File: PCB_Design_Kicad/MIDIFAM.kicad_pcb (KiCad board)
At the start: 2 copper layers, 58 x 87.2 mm, 61 parts, among them IC1 DAC8562SDGSR, J1 PWR_IN, J10 midi, J11 back bottom, J12 front bottom, J13 back top, J14 front top, J2 ISP connector, J3 Voct_A, J4 Trig_A, J5 Vel_A, J6 Voct_B, J7 Trig_B, J8 Vel_B, J9 adv_clock_out, SW1 re-sync, SW2 midi learn, SW3 seq. mode, U1 TL072, U2 MCP1703Ax-500xxDB, U5 6N137, U6 ATmega328-A

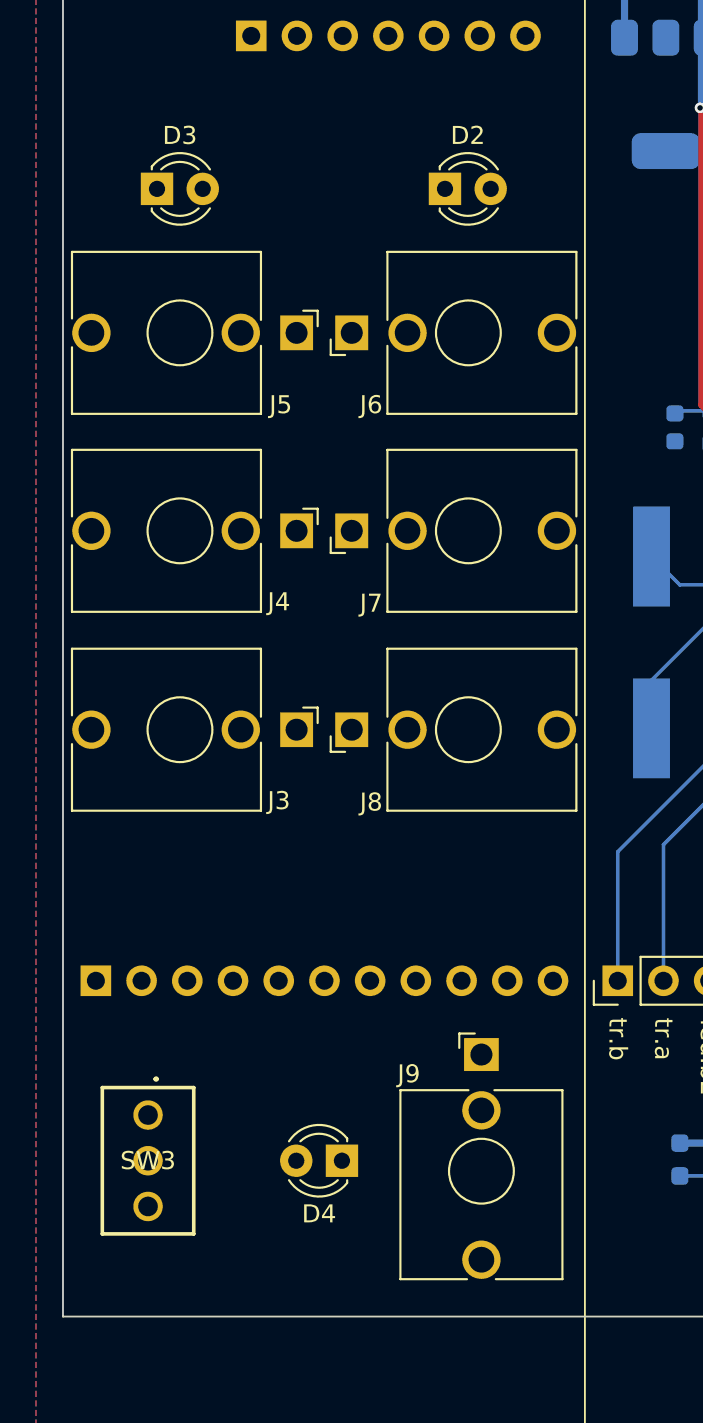
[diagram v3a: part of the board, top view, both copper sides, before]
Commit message: fix footprints and jack position
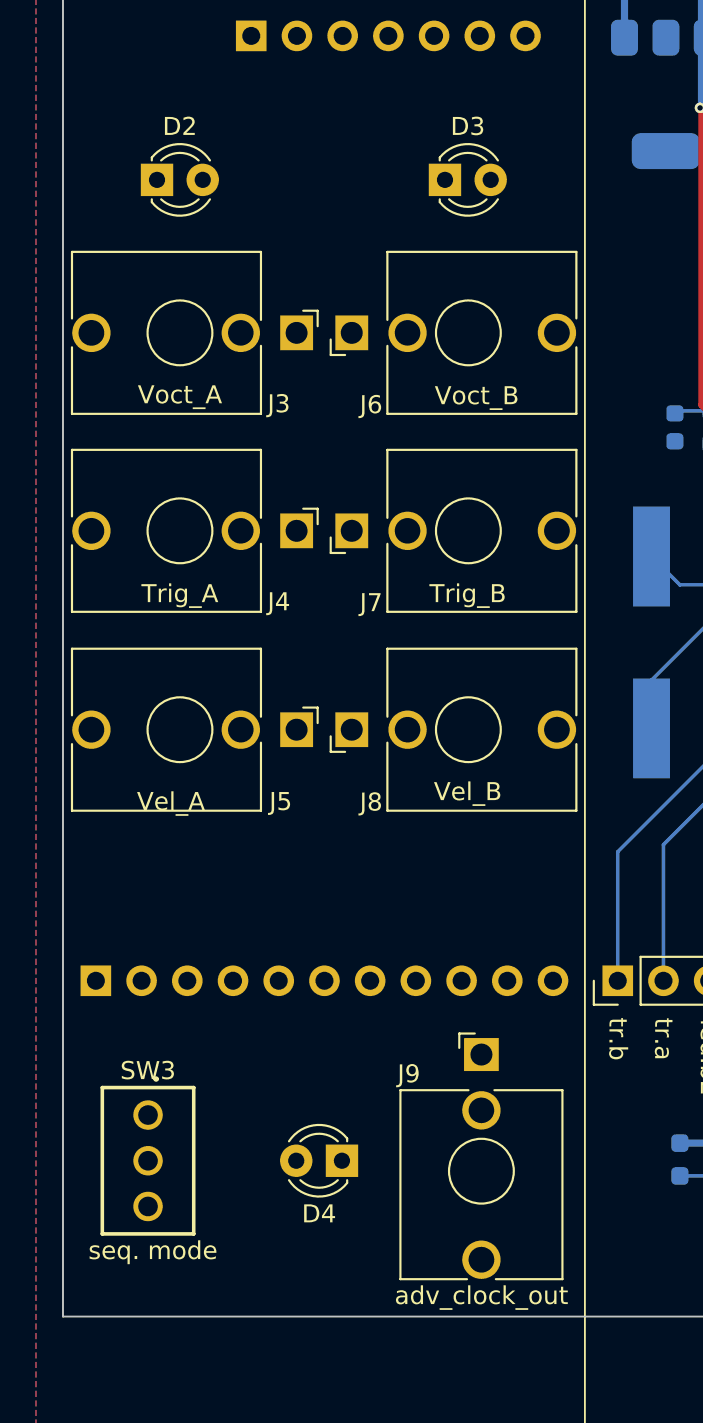
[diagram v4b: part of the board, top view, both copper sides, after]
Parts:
- moved J3 22.0 mm to (61.3, 57.5)
- moved J5 22.0 mm to (61.3, 79.5)
- moved D2 16.0 mm to (60.0, 49.0)
- moved D3 16.0 mm to (76.0, 49.0)

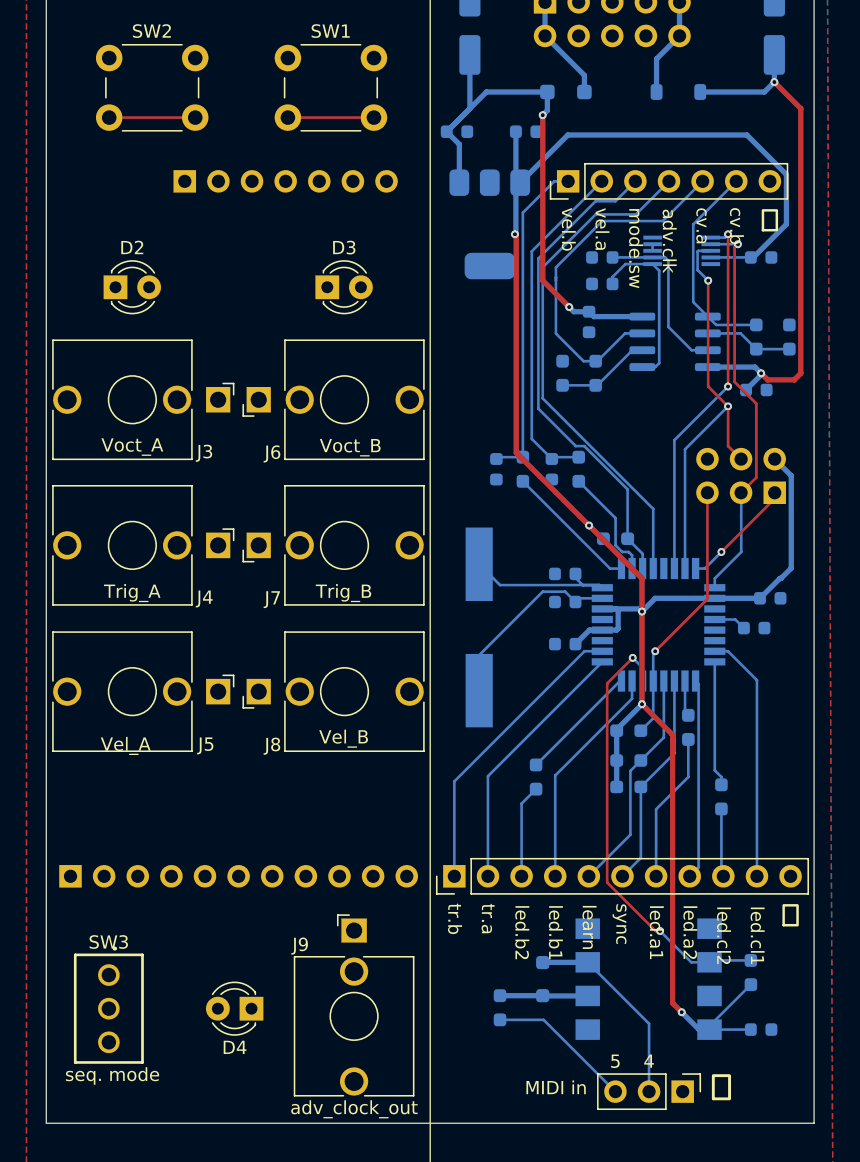
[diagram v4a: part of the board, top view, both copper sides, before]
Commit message: good routing and ground planes
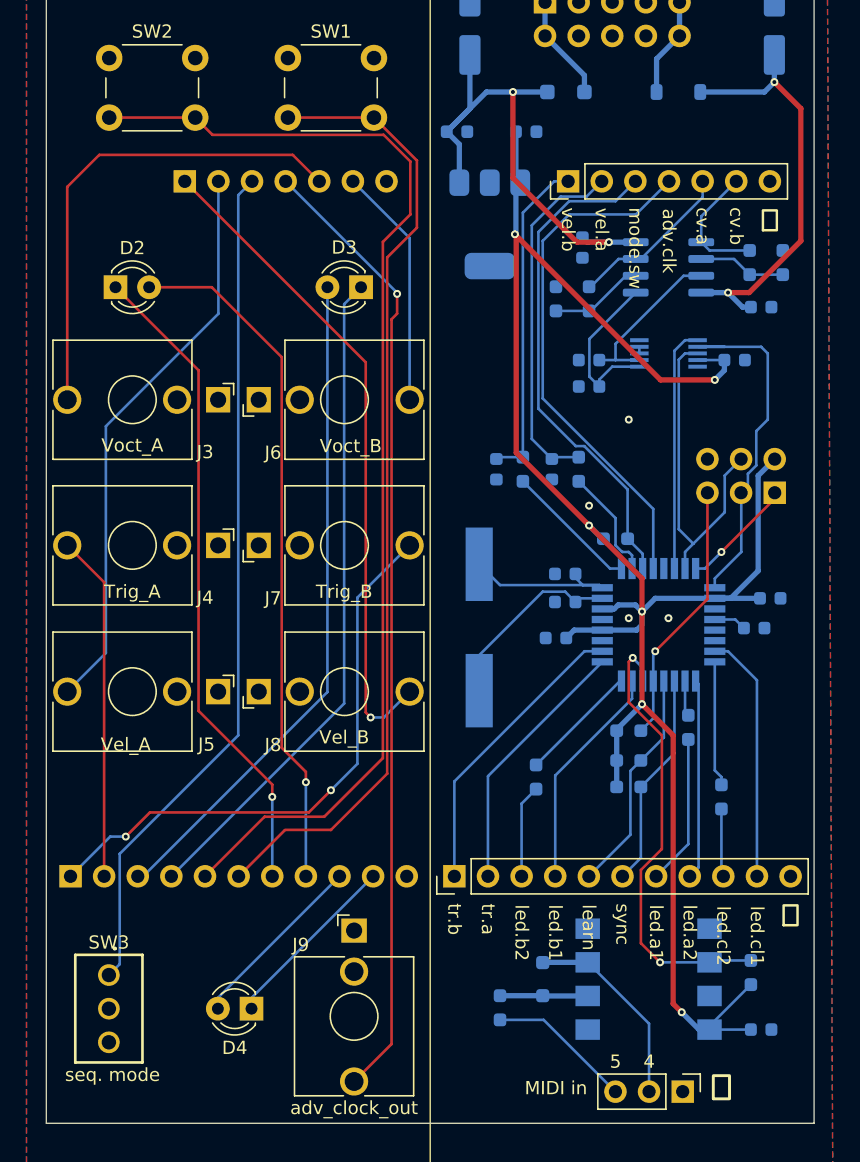
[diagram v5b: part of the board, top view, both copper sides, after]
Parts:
- moved C17 8.00 mm to (106.8, 54.5)
- moved C4 7.81 mm to (95.8, 56.5)
- moved C5 7.81 mm to (95.8, 54.5)
- moved IC1 7.81 mm to (101.8, 54.0)
- moved C12 6.27 mm to (108.8, 50.5)
- moved C10 5.65 mm to (95.3, 46.0)
- moved R1 5.65 mm to (95.8, 49.9)
- moved R2 5.65 mm to (93.3, 49.9)
- moved R3 5.65 mm to (107.9, 47.1)
- moved R4 5.65 mm to (110.4, 47.1)
- moved U1 5.65 mm to (101.8, 47.5)
- moved D3 2.55 mm to (78.5, 49.0), turned to 180 degrees
- moved C1 0.84 mm to (93.3, 75.5)
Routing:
- net /IO Control PCB/learn_sw_f: track 6.50 -> 87.2 mm
- net /IO Control PCB/adv_clock_f: track 0.00 -> 72.8 mm, vias 0 -> 1
- net /IO Control PCB/sync_sw_f: track 6.50 -> 72.8 mm
- net /IO Control PCB/seq_mode_sw: track 0.00 -> 64.4 mm
- net /IO Control PCB/led_a2_f: track 0.00 -> 52.2 mm, vias 0 -> 1
- net /IO Control PCB/led_b2_f: track 0.00 -> 50.7 mm
- net /IO Control PCB/led_b1_f: track 0.00 -> 50.4 mm
- net /IO Control PCB/vel_b_f: track 0.00 -> 50.1 mm, vias 0 -> 1
- net /IO Control PCB/led_a1_f: track 0.00 -> 49.4 mm, vias 0 -> 1
- net /IO Control PCB/trig_b_f: track 0.00 -> 43.3 mm, vias 0 -> 2
- net /IO Control PCB/vel_a_f: track 0.00 -> 43.3 mm
- net /IO Control PCB/voct_a_f: track 0.00 -> 37.0 mm
- net /IO Control PCB/trig_a_f: track 0.00 -> 26.2 mm
- net /IO Control PCB/voct_b_f: track 0.00 -> 18.3 mm
- net /voct_a_b: track 27.3 -> 12.6 mm
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
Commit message: ready for schematic review
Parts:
- removed C4, C5: 1u, Capacitor_SMD:C_0603_1608Metric
- added C18: 18p, Capacitor_SMD:C_0603_1608Metric, B.Cu at (95.8, 49.5)
- added C19: 18p, Capacitor_SMD:C_0603_1608Metric, B.Cu at (107.8, 48.0)
- added R16: 47k, Resistor_SMD:R_0603_1608Metric_Pad0.98x0.95mm_HandSolder, B.Cu at (95.8, 55.0)
- added R17: 47k, Resistor_SMD:R_0603_1608Metric_Pad0.98x0.95mm_HandSolder, B.Cu at (95.8, 53.0)
- added R18: 1k, Resistor_SMD:R_0603_1608Metric_Pad0.98x0.95mm_HandSolder, B.Cu at (103.3, 43.5)
- added R19: 1k, Resistor_SMD:R_0603_1608Metric_Pad0.98x0.95mm_HandSolder, B.Cu at (106.8, 44.5)
- R1, R3: value ? -> 240k
- R2, R4: value ? -> 47k
- moved R2 8.85 mm to (97.8, 57.5)
- moved R1 8.68 mm to (103.3, 45.5), turned to 180 degrees
- moved R4 6.65 mm to (107.3, 53.0), turned to 180 degrees
- moved R3 2.48 mm to (109.8, 45.5), turned to -90 degrees
- moved C17 2.06 mm to (107.3, 56.5)
- moved IC1 2.06 mm to (102.3, 56.0)
- moved U1 2.06 mm to (102.3, 49.5)
- moved C12 1.12 mm to (109.3, 51.5)
- moved C10 1.00 mm to (95.3, 47.0), turned to 180 degrees
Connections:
- R1 pad 1: Net-(U1B--) -> /voct_a_b
- R1 pad 2: /voct_a_b -> Net-(U1B--)
- R2 pad 1: GND -> Net-(U1B--)
- R2 pad 2: Net-(U1B--) -> /DAC_OUT_A
- R3 pad 1: Net-(U1A--) -> /voct_b_b
- R3 pad 2: /voct_b_b -> Net-(U1A--)
- R4 pad 1: GND -> Net-(U1A--)
- R4 pad 2: Net-(U1A--) -> /DAC_OUT_B
- U1 pad 1: /voct_b_b -> Net-(C19-Pad2)
- U1 pad 3: /DAC_OUT_B -> /VREF/2
- U1 pad 5: /DAC_OUT_A -> /VREF/2
- U1 pad 7: /voct_a_b -> Net-(C18-Pad2)
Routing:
- net Net-(U1B--): track 6.38 -> 20.4 mm
- net 5V: track 146.7 -> 132.7 mm
- net /VREF/2: track 0.00 -> 13.1 mm
- net Net-(C18-Pad2): track 0.00 -> 11.1 mm
- net /DAC_OUT_A: track 12.8 -> 2.89 mm
- net /VREF_DAC: track 0.00 -> 8.62 mm, vias 0 -> 2
- net /voct_a_b: track 12.6 -> 4.57 mm
- net Net-(C19-Pad2): track 0.00 -> 7.23 mm
- net /SCK: track 26.9 -> 20.5 mm
- net /MOSI: track 26.1 -> 20.5 mm
- net Net-(U1A--): track 6.65 -> 11.8 mm
- net /DAC_OUT_B: track 12.9 -> 7.74 mm
- net /voct_b_b: track 9.61 -> 5.95 mm
- net /CS: track 18.5 -> 17.4 mm
- net +12V: track 39.5 -> 40.2 mm
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
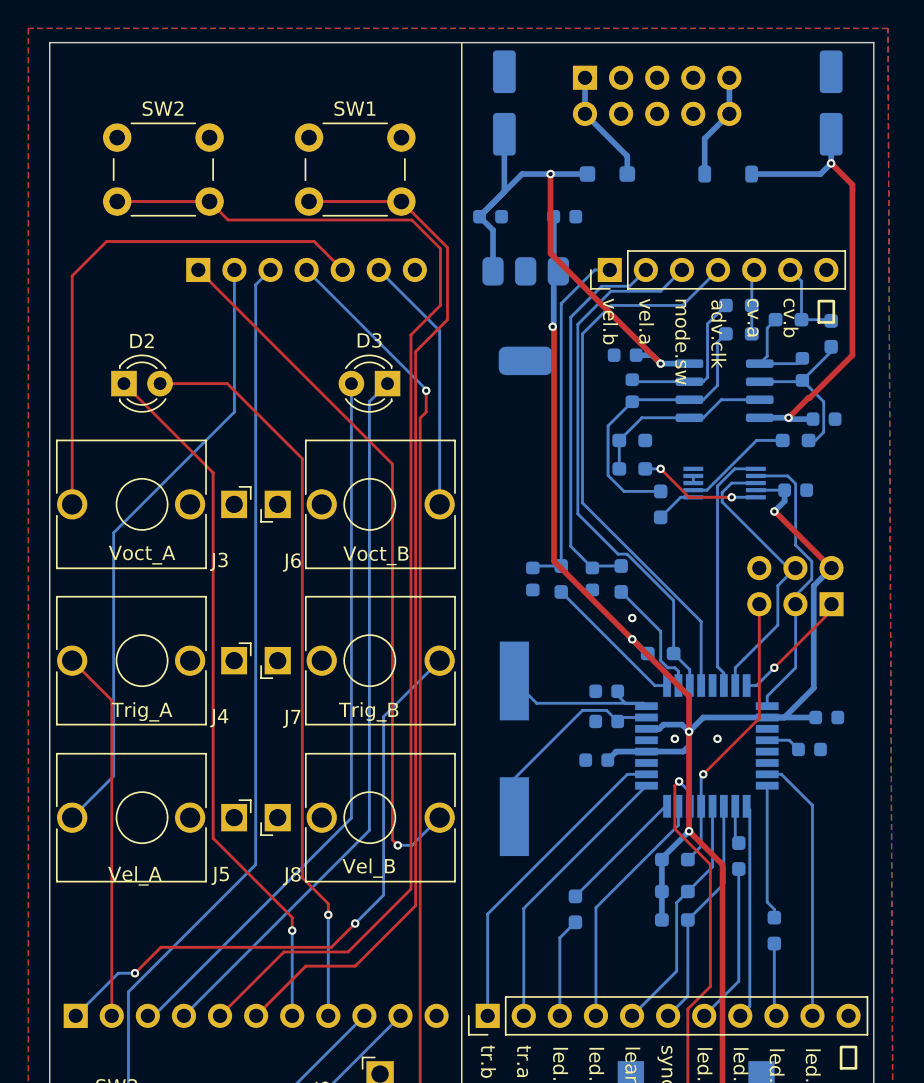
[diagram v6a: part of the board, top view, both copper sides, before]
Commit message: op amps for velocity!
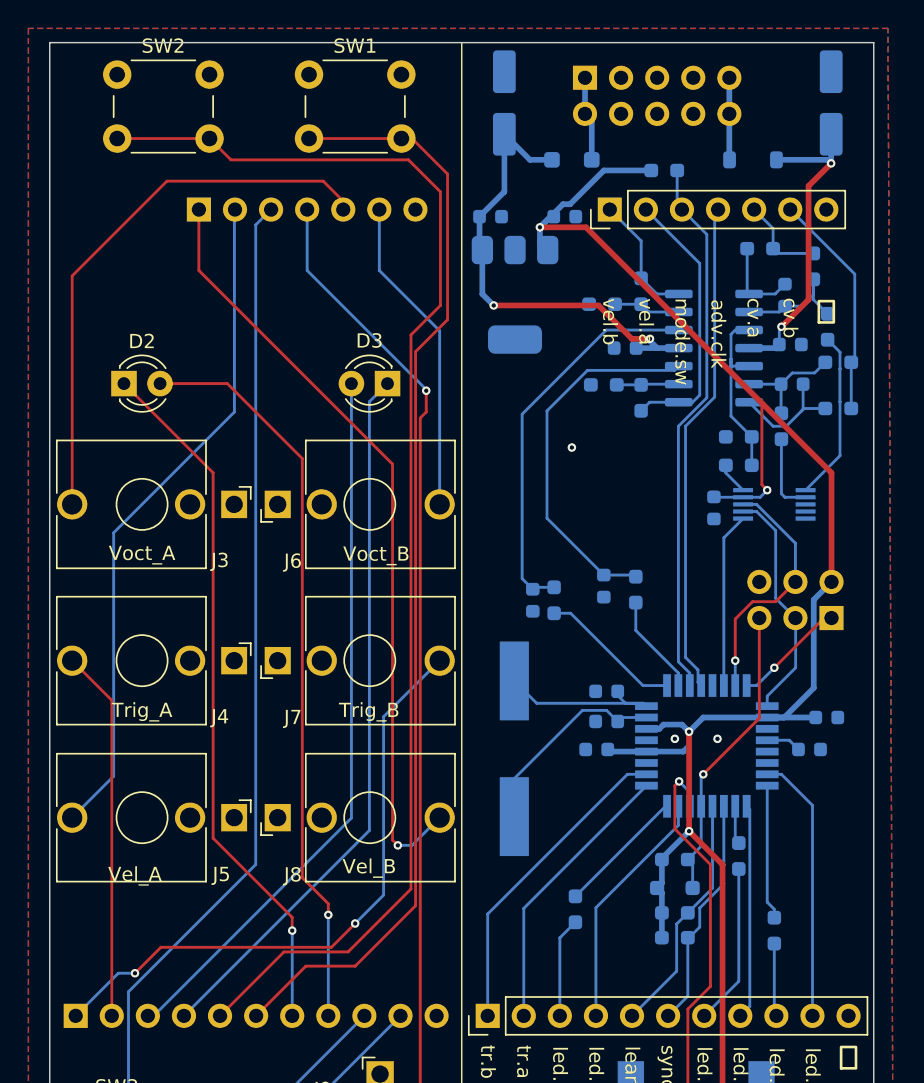
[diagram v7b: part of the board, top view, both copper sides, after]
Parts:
- removed C18, C19: 18p, Capacitor_SMD:C_0603_1608Metric
- removed U1: TL072, Package_SO:SOIC-8_3.9x4.9mm_P1.27mm
- added C4: ??, Capacitor_SMD:C_0603_1608Metric, B.Cu at (88.8, 64.2)
- added C5: 18p, Capacitor_SMD:C_0603_1608Metric, B.Cu at (106.5, 42.8)
- added D7: 1N4148, Diode_SMD:D_SOD-323_HandSoldering, B.Cu at (98.8, 84.5)
- added R20: 6k, Resistor_SMD:R_0603_1608Metric_Pad0.98x0.95mm_HandSolder, B.Cu at (96.4, 42.5)
- added R21: 10k, Resistor_SMD:R_0603_1608Metric_Pad0.98x0.95mm_HandSolder, B.Cu at (93.7, 43.4)
- added R22: 6k, Resistor_SMD:R_0603_1608Metric_Pad0.98x0.95mm_HandSolder, B.Cu at (96.4, 50.0)
- added R23: 10k, Resistor_SMD:R_0603_1608Metric_Pad0.98x0.95mm_HandSolder, B.Cu at (93.8, 49.1)
- added U4: OPA4196xD, Package_SO:SOIC-14_3.9x8.7mm_P1.27mm, B.Cu at (101.5, 46.5)
- C16: value ?? -> 18p
- moved R15 34.0 mm to (98.0, 34.0)
- moved C16 22.8 mm to (107.0, 49.0), turned to 0 degrees
- moved R2 17.2 mm to (109.5, 45.0)
- moved R17 7.50 mm to (103.3, 52.8), turned to 0 degrees
- moved R16 7.50 mm to (103.3, 54.8), turned to 180 degrees
- moved R19 7.16 mm to (110.3, 50.8)
- moved R1 7.08 mm to (108.5, 40.8), turned to -90 degrees
- moved C17 5.88 mm to (101.5, 57.8), turned to -90 degrees
- moved C12 5.76 mm to (106.9, 46.2)
- moved SW1 4.43 mm to (73.0, 27.2)
- moved SW2 4.43 mm to (59.5, 27.2)
- moved R18 4.27 mm to (104.8, 39.5)
- moved J14 4.25 mm to (65.3, 36.8)
- moved J13 4.25 mm to (94.2, 36.8)
- moved IC1 3.81 mm to (105.8, 57.5), turned to 180 degrees
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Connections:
- C15 pad 2: /vel_a_b -> Net-(U4A-+)
- C16 pad 1: GND -> Net-(U4D--)
- C16 pad 2: /vel_b_b -> Net-(C16-Pad2)
- R19 pad 2: Net-(C19-Pad2) -> Net-(C16-Pad2)
- R3 pad 2: Net-(U1A--) -> Net-(U4D--)
- R4 pad 1: Net-(U1A--) -> Net-(U4D--)
- R6 pad 2: /vel_a_b -> Net-(U4A-+)
- R9 pad 2: /vel_b_b -> Net-(U4B-+)
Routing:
- net Net-(U4B-+): track 0.00 -> 27.7 mm
- net Net-(U4A-+): track 0.00 -> 26.1 mm
- net /vel_b_b: track 24.7 -> 8.86 mm
- net Net-(U1A--): track 11.8 -> 0.00 mm
- net Net-(U4C--): track 20.4 -> 8.95 mm
- net /voct_b_b: track 5.95 -> 16.0 mm
- net -12V: track 32.2 -> 22.4 mm
- net /DAC_OUT_A: track 2.89 -> 12.0 mm
- net Net-(C16-Pad2): track 0.00 -> 8.50 mm
- net Net-(U4D--): track 0.00 -> 8.06 mm
- net /vel_a_b: track 26.8 -> 19.2 mm
- net 5V: track 132.7 -> 140.1 mm, vias 6 -> 5
- net Net-(C19-Pad2): track 7.23 -> 0.00 mm
- net +12V: track 40.2 -> 33.1 mm
- net /VREF_DAC: track 8.62 -> 2.25 mm, vias 2 -> 0
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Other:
- board text added: "ISP"
- board text removed: "ISP conn."
